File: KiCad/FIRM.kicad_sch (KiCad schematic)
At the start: 98 parts, among them J1 Conn_01x02_Pin, J2 DM3CS-SF, Q2 IRLML6402, SW1 PTS815, U1 STM32F405RGTx, U2 MIC5219-3.3YM5, U6 A-USBC-20F0-EA-GSR05, U7 W25Q128JVS, X2 32.768khz, Y1 12 MHz

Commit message: Finish part numbers
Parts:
- C1, C15, C19, C2, C20, C21, C25, C26, C27, C3, C4, C5, C8: LCSC PN  C1590 -> (none); MPN (none) -> C1590
- C10, C9: LCSC PN  C1607 -> (none); MPN (none) -> C1607
- C11, C12: LCSC PN  C37474 -> (none); MPN (none) -> C37474
- C13, C14: LCSC PN  C5360816 -> (none); MPN (none) -> C5360816
- C16, C18: LCSC PN  C1592 -> (none); MPN (none) -> C1592
- C17, C22, C24: LCSC PN  C1691 -> (none); MPN (none) -> C1691
- C23: LCSC PN  C1620 -> (none); MPN (none) -> C1620
- C6: LCSC PN  C1705 -> (none); MPN (none) -> C1705
- C7: LCSC PN  C1589 -> (none); MPN (none) -> C1589
- D1: LCSC PN  C82544 -> (none); MPN (none) -> C82544
- D2: LCSC PN  C2293 -> (none); MPN (none) -> C2293
- D3: LCSC PN  C2296 -> (none); MPN (none) -> C2296
- D4: LCSC PN  C84256 -> (none); MPN (none) -> C84256
- D5: LCSC PN  C2297 -> (none); MPN (none) -> C2297
- FB1: LCSC PN  C3716596 -> (none); MPN (none) -> C3716596
- J2: LCSC PN  C202111 -> (none); MPN (none) -> C202111
- Q2: LCSC PN  C22367042 -> (none); MPN (none) -> C22367042
- R1, R8: LCSC PN  C177329 -> (none); MPN (none) -> C177329
- R10: LCSC PN  C177341 -> (none); MPN (none) -> C177341
- R11, R15: LCSC PN  C22369820 -> (none); MPN (none) -> C22369820
- R12: LCSC PN  C22369819 -> (none); MPN (none) -> C22369819
- R13, R14, R21, R7: LCSC PN  C22356465 -> (none); MPN (none) -> C22356465
- R18, R19: LCSC PN  C22356633 -> (none); MPN (none) -> C22356633
- R2, R3, R4, R5, R6: LCSC PN  C177336 -> (none); MPN (none) -> C177336
- R20: LCSC PN  C177347 -> (none); MPN (none) -> C177347
- R22, R9: LCSC PN  C177348 -> (none); MPN (none) -> C177348
- SW1: LCSC PN  C411883 -> (none); MPN (none) -> C411883
- U1: LCSC PN  C15742 -> (none); MPN (none) -> C15742
- U2: LCSC PN  C5370977 -> (none); MPN (none) -> C5370977
- U3: LCSC PN  C22459454 -> (none); MPN (none) -> C22459454
- U4: LCSC PN  C404329 -> (none); MPN (none) -> C404329
- U5: LCSC PN  C5362283 -> (none); MPN (none) -> C5362283
- U6: LCSC PN  C22036153 -> (none); MPN (none) -> C22036153
- U7: LCSC PN  C97521 -> (none); MPN (none) -> C97521
- X2: LCSC PN  C2450425 -> (none); MPN (none) -> C2450425
- Y1: LCSC PN  C20625731 -> (none); MPN (none) -> C20625731
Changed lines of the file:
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@@
 			)
 		)
-		(property "LCSC PN " "C1590"
+		(property "MPN" "C1590"
 			(at 87.63 41.91 0)
 			(effects
@@
 			)
 		)
-		(property "LCSC PN " "C1590"
+		(property "MPN" "C1590"
 			(at 36.83 41.91 0)
 			(effects
@@
 			)
 		)
-		(property "LCSC PN " "C22356465"
+		(property "MPN" "C22356465"
 			(at 22.86 255.27 0)
 			(effects
@@
 			)
 		)
-		(property "LCSC PN " "C177329"
+		(property "MPN" "C177329"
 			(at 30.48 66.04 0)
 			(effects
@@
 			)
 		)
-		(property "LCSC PN " "C1691"
+		(property "MPN" "C1691"
 			(at 308.61 224.79 0)
 			(effects
@@
 			)
 		)
-		(property "LCSC PN " "C97521"
+		(property "MPN" "C97521"
 			(at 60.96 260.35 0)
 			(effects
@@
 			)
 		)
-		(property "LCSC PN " "C1590"
+		(property "MPN" "C1590"
 			(at 19.05 60.96 0)
 			(effects
@@
 			)
 		)
-		(property "LCSC PN " "C177336"
+		(property "MPN" "C177336"
 			(at 52.07 177.8 0)
 			(effects
@@
 			)
 		)
-		(property "LCSC PN " "C2296"
+		(property "MPN" "C2296"
 			(at 184.15 119.38 0)
 			(effects
@@
 			)
 		)
-		(property "LCSC PN " "C404329"
+		(property "MPN" "C404329"
 			(at 325.12 111.76 0)
 			(effects
@@
 			)
 		)
-		(property "LCSC PN " "C1590"
+		(property "MPN" "C1590"
 			(at 64.77 195.58 0)
 			(effects
@@
 			)
 		)
-		(property "LCSC PN " "C177336"
+		(property "MPN" "C177336"
 			(at 59.69 177.8 0)
 			(effects
@@
 			)
 		)
-		(property "LCSC PN " "C177336"
+		(property "MPN" "C177336"
 			(at 25.4 177.8 0)
 			(effects
@@
 			)
 		)
-		(property "LCSC PN " "C22356633"
+		(property "MPN" "C22356633"
 			(at 153.67 111.76 0)
 			(effects
@@
 			)
 		)
-		(property "LCSC PN " "C22356465"
+		(property "MPN" "C22356465"
 			(at 38.1 212.09 90)
 			(effects
@@
 			)
 		)
-		(property "LCSC PN " "C1590"
+		(property "MPN" "C1590"
 			(at 66.04 240.03 90)
 			(effects
@@
 			)
 		)
-		(property "LCSC PN " "C5360816"
+		(property "MPN" "C5360816"
 			(at 41.91 88.9 0)
 			(effects
@@
 			)
 		)
-		(property "LCSC PN " "C1590"
+		(property "MPN" "C1590"
 			(at 142.24 41.91 0)
 			(effects
@@
 			)
 		)
-		(property "LCSC PN " "C84256"
+		(property "MPN" "C84256"
 			(at 184.15 130.81 0)
 			(effects
@@
 			)
 		)
-		(property "LCSC PN " "C177341"
+		(property "MPN" "C177341"
 			(at 170.18 107.95 90)
 			(effects
@@
 			)
 		)
-		(property "LCSC PN " "C22356633"
+		(property "MPN" "C22356633"
 			(at 144.78 111.76 0)
 			(effects
@@
 			)
 		)
-		(property "LCSC PN " "C5360816"
+		(property "MPN" "C5360816"
 			(at 63.5 90.17 0)
 			(effects
@@
 			)
 		)
-		(property "LCSC PN " "C22369820"
+		(property "MPN" "C22369820"
 			(at 290.83 208.28 0)
 			(effects
@@
 			)
 		)
-		(property "LCSC PN " "C22369819"
+		(property "MPN" "C22369819"
 			(at 170.18 130.81 90)
 			(effects
@@
 			)
 		)
-		(property "LCSC PN " "C37474"
+		(property "MPN" "C37474"
 			(at 39.37 130.81 0)
 			(effects
@@
 			)
 		)
-		(property "LCSC PN " "C177336"
+		(property "MPN" "C177336"
 			(at 44.45 177.8 0)
 			(effects
@@
 			)
 		)
-		(property "LCSC PN " "C1691"
+		(property "MPN" "C1691"
 			(at 317.5 138.43 90)
 			(effects
@@
 			)
 		)
-		(property "LCSC PN " "C177347"
+		(property "MPN" "C177347"
 			(at 379.73 53.34 90)
 			(effects
@@
 			)
 		)
-		(property "LCSC PN " "C22356465"
+		(property "MPN" "C22356465"
 			(at 39.37 245.11 0)
 			(effects
@@
 			)
 		)
-		(property "LCSC PN " "C1607"
+		(property "MPN" "C1607"
 			(at 73.66 130.81 0)
 			(effects
@@
 			)
 		)
-		(property "LCSC PN " "C1592"
+		(property "MPN" "C1592"
 			(at 172.72 41.91 0)
 			(effects
@@
 			)
 		)
-		(property "LCSC PN " "C1590"
+		(property "MPN" "C1590"
 			(at 327.66 27.94 90)
 			(effects
@@
 			)
 		)
-		(property "LCSC PN " "C1589"
+		(property "MPN" "C1589"
 			(at 130.81 41.91 0)
 			(effects
@@
 			)
 		)
-		(property "LCSC PN " "C2450425"
+		(property "MPN" "C2450425"
 			(at 44.45 121.92 0)
 			(effects
@@
 			)
 		)
-		(property "LCSC PN " "C22036153"
+		(property "MPN" "C22036153"
 			(at 345.44 204.47 0)
 			(effects
@@
 			)
 		)
-		(property "LCSC PN " "C37474"
+		(property "MPN" "C37474"
 			(at 50.8 130.81 0)
 			(effects
@@
 			)
 		)
-		(property "LCSC PN " "C177329"
+		(property "MPN" "C177329"
 			(at 243.84 222.25 0)
 			(effects
@@
 			)
 		)
-		(property "LCSC PN " "C3716596"
+		(property "MPN" "C3716596"
 			(at 154.94 36.83 90)
 			(effects
@@
 			)
 		)
-		(property "LCSC PN " "C20625731"
+		(property "MPN" "C20625731"
 			(at 52.07 81.28 0)
 			(effects
@@
 			)
 		)
-		(property "LCSC PN " "C2297"
+		(property "MPN" "C2297"
 			(at 294.64 201.93 0)
 			(effects
@@
 			)
 		)
-		(property "LCSC PN " "C82544"
+		(property "MPN" "C82544"
 			(at 252.73 214.63 0)
 			(effects
@@
 			)
 		)
-		(property "LCSC PN " "C1590"
+		(property "MPN" "C1590"
 			(at 48.26 41.91 0)
 			(effects
@@
 			)
 		)
-		(property "LCSC PN " "C1691"
+		(property "MPN" "C1691"
 			(at 261.62 224.79 0)
 			(effects
@@
 			)
 		)
-		(property "LCSC PN " "C177336"
+		(property "MPN" "C177336"
 			(at 33.02 177.8 0)
 			(effects
@@
 			)
 		)
-		(property "LCSC PN " "C5362283"
+		(property "MPN" "C5362283"
 			(at 327.66 48.26 0)
 			(effects
@@
 			)
 		)
-		(property "LCSC PN " "C2293"
+		(property "MPN" "C2293"
 			(at 184.15 107.95 0)
 			(effects
@@
 			)
 		)
-		(property "LCSC PN " "C1590"
+		(property "MPN" "C1590"
 			(at 320.04 27.94 90)
 			(effects
@@
 			)
 		)
-		(property "LCSC PN " "C15742"
+		(property "MPN" "C15742"
 			(at 106.68 96.52 0)
 			(effects
@@
 			)
 		)
-		(property "LCSC PN " "C177348"
+		(property "MPN" "C177348"
 			(at 373.38 198.12 90)
 			(effects
@@
 			)
 		)
-		(property "LCSC PN " "C5370977"
+		(property "MPN" "C5370977"
 			(at 280.67 217.17 0)
 			(effects
@@
 			)
 		)
-		(property "LCSC PN " "C177348"
+		(property "MPN" "C177348"
 			(at 367.03 195.58 90)
 			(effects
@@
 			)
 		)
-		(property "LCSC PN " "C1592"
+		(property "MPN" "C1592"
 			(at 314.96 148.59 0)
 			(effects
@@
 			)
 		)
-		(property "LCSC PN " "C1590"
+		(property "MPN" "C1590"
 			(at 73.66 41.91 0)
 			(effects
@@
 			)
 		)
-		(property "LCSC PN " "C1705"
+		(property "MPN" "C1705"
 			(at 22.86 41.91 0)
 			(effects
@@
 			)
 		)
-		(property "LCSC PN " "C22369820"
+		(property "MPN" "C22369820"
 			(at 170.18 119.38 90)
 			(effects
@@
 			)
 		)
-		(property "LCSC PN " "C22459454"
+		(property "MPN" "C22459454"
 			(at 251.46 55.88 0)
 			(effects
@@
 			)
 		)
-		(property "LCSC PN " "C22367042"
+		(property "MPN" "C22367042"
 			(at 259.08 201.93 0)
 			(effects
@@
 			)
 		)
-		(property "LCSC PN " "C1590"
+		(property "MPN" "C1590"
 			(at 254 76.2 0)
 			(effects
@@
 			)
 		)
-		(property "LCSC PN " "C1607"
+		(property "MPN" "C1607"
 			(at 62.23 130.81 0)
 			(effects
@@
 			)
 		)
-		(property "LCSC PN " "C202111"
+		(property "MPN" "C202111"
 			(at 96.52 196.85 0)
 			(effects
@@
 			)
 		)
-		(property "LCSC PN " "C1590"
+		(property "MPN" "C1590"
 			(at 60.96 41.91 0)
 			(effects
@@
 			)
 		)
-		(property "LCSC PN " "C22356465"
+		(property "MPN" "C22356465"
 			(at 33.02 255.27 0)
 			(effects
@@
 			)
 		)
-		(property "LCSC PN " "C411883"
+		(property "MPN" "C411883"
 			(at 382.27 31.75 0)
 			(effects
@@
 			)
 		)
-		(property "LCSC PN " "C1620"
+		(property "MPN" "C1620"
 			(at 290.83 222.25 0)
 			(effects
@@
 			)
 		)
-		(property "LCSC PN " "C1590"
+		(property "MPN" "C1590"
 			(at 264.16 76.2 0)
 			(effects

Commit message: bom digikey
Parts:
- C1, C15, C19, C2, C20, C21, C25, C26, C27, C3, C4, C5, C8: Digikey PN (none) -> 399-C0603C104K5RACTUCT-ND
- C10, C9: Digikey PN (none) -> 490-4520-1-ND
- C11, C12: Digikey PN (none) -> 1276-2134-1-ND
- C13, C14: Digikey PN (none) -> 311-1767-1-ND
- C16, C18: Digikey PN (none) -> 1276-1184-1-ND
- C17, C22, C24: Digikey PN (none) -> 490-18214-1-ND
- C23: Digikey PN (none) -> 1276-1168-1-ND
- C6: Digikey PN (none) -> 1276-1044-1-ND
- C7: Digikey PN (none) -> 399-C0603C103K5RACTUCT-ND
- D1: Digikey PN (none) -> 1N5819HW-FDICT-ND
- D2: Digikey PN (none) -> 160-1645-1-ND
- D3: Digikey PN (none) -> 160-1428-1-ND
- D4: Digikey PN (none) -> 160-1422-1-ND
- D5: Digikey PN (none) -> 160-1423-1-ND
- FB1: Digikey PN (none) -> 1934-1472-1-ND
- J2: Digikey PN (none) -> HR1972CT-ND
- Q2: Digikey PN (none) -> IRLML6402PBFCT-ND
- R1, R8: Digikey PN (none) -> 311-100KHRCT-ND
- R10: Digikey PN (none) -> 311-330HRCT-ND
- R11, R15: Digikey PN (none) -> P1.2KDBCT-ND
- R12: Digikey PN (none) -> 311-1.50KHRCT-ND
- R13, R14, R21, R7: Digikey PN (none) -> 311-10.0KHRCT-ND
- R18, R19: Digikey PN (none) -> 311-2.20KHRCT-ND
- R2, R3, R4, R5, R6: Digikey PN (none) -> 311-47.0KHRCT-ND
- R20: Digikey PN (none) -> 541-100HCT-ND
- R22, R9: Digikey PN (none) -> 311-5.10KHRCT-ND
- SW1: Digikey PN (none) -> CKN12215-1-ND
- U1: Digikey PN (none) -> 497-11767-ND
- U2: Digikey PN (none) -> 576-1281-1-ND
- U3: Digikey PN (none) -> 1428-ICM-45686CT-ND
- U4: Digikey PN (none) -> 1267-MMC5983MACT-ND
- U5: Digikey PN (none) -> 828-BMP581CT-ND
- U6: Digikey PN (none) -> 123-A-USBC-20F0-EA-GSR05CT-ND
- U7: Digikey PN (none) -> 256-W25Q128JVSIQTRCT-ND
- X2: Digikey PN (none) -> 50-ECS-.327-6-34R-TRCT-ND
- Y1: Digikey PN (none) -> 535-ABM8-272-T3CT-ND

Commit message: update bom
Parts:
- C16, C18: Digikey PN 1276-1184-1-ND -> 1276-1029-1-ND
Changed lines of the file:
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@@
 			)
 		)
-		(property "Digikey PN" "1276-1184-1-ND"
+		(property "Digikey PN" "1276-1029-1-ND"
 			(at 172.72 41.91 0)
 			(effects
@@
 			)
 		)
-		(property "Digikey PN" "1276-1184-1-ND"
+		(property "Digikey PN" "1276-1029-1-ND"
 			(at 314.96 148.59 0)
 			(effects

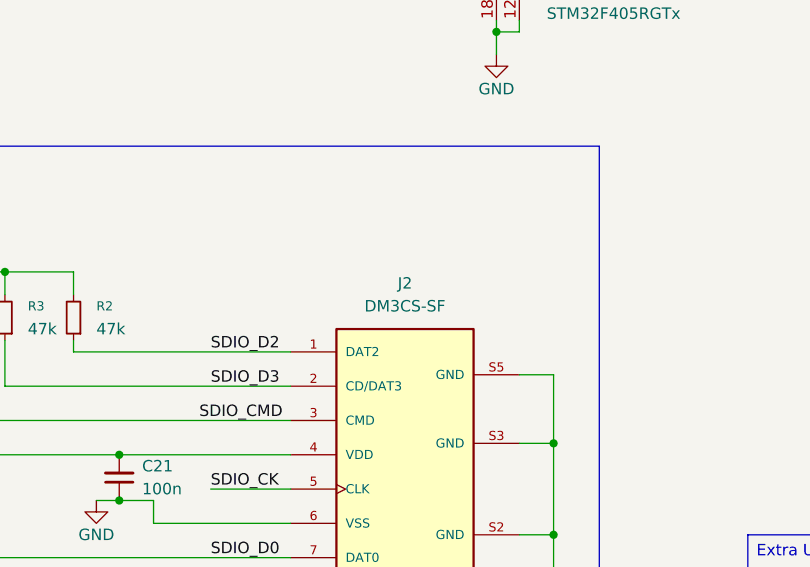
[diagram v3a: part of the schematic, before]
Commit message: fix fb and cap
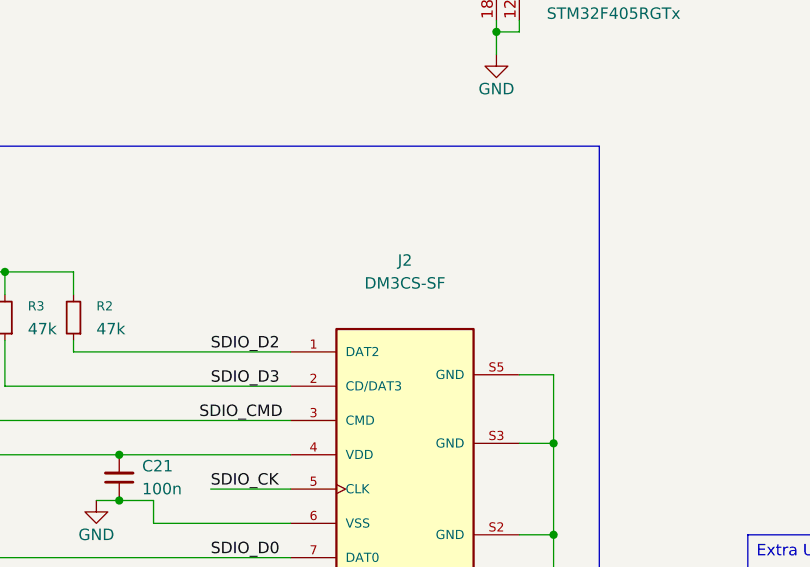
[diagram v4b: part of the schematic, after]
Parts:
- C16, C18: Digikey PN 1276-1029-1-ND -> 587-1241-1-ND
- FB1: footprint Inductor_SMD:L_1206_3216Metric -> Inductor_SMD:L_0805_2012Metric
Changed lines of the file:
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@@
 			)
 		)
-		(property "Digikey PN" "1276-1029-1-ND"
+		(property "Digikey PN" "587-1241-1-ND"
 			(at 172.72 41.91 0)
 			(effects
@@
 			)
 		)
-		(property "Footprint" "Inductor_SMD:L_1206_3216Metric"
+		(property "Footprint" "Inductor_SMD:L_0805_2012Metric"
 			(at 154.94 38.608 90)
 			(effects
@@
 			)
 		)
-		(property "Digikey PN" "1276-1029-1-ND"
+		(property "Digikey PN" "587-1241-1-ND"
 			(at 314.96 148.59 0)
 			(effects
@@
 		(fields_autoplaced yes)
 		(property "Reference" "J2"
-			(at 96.52 173.99 0)
+			(at 96.52 171.45 0)
 			(effects
 				(font
@@
 		)
 		(property "Value" "DM3CS-SF"
-			(at 96.52 176.53 0)
+			(at 96.52 173.99 0)
 			(effects
 				(font
@@
 		)
 		(property "Footprint" "DM3CS-SF:HRS_DM3CS-SF"
-			(at 96.52 196.85 0)
+			(at 96.52 176.53 0)
 			(effects
 				(font
 					(size 1.27 1.27)
 				)
-				(justify bottom)
 				(hide yes)
 			)

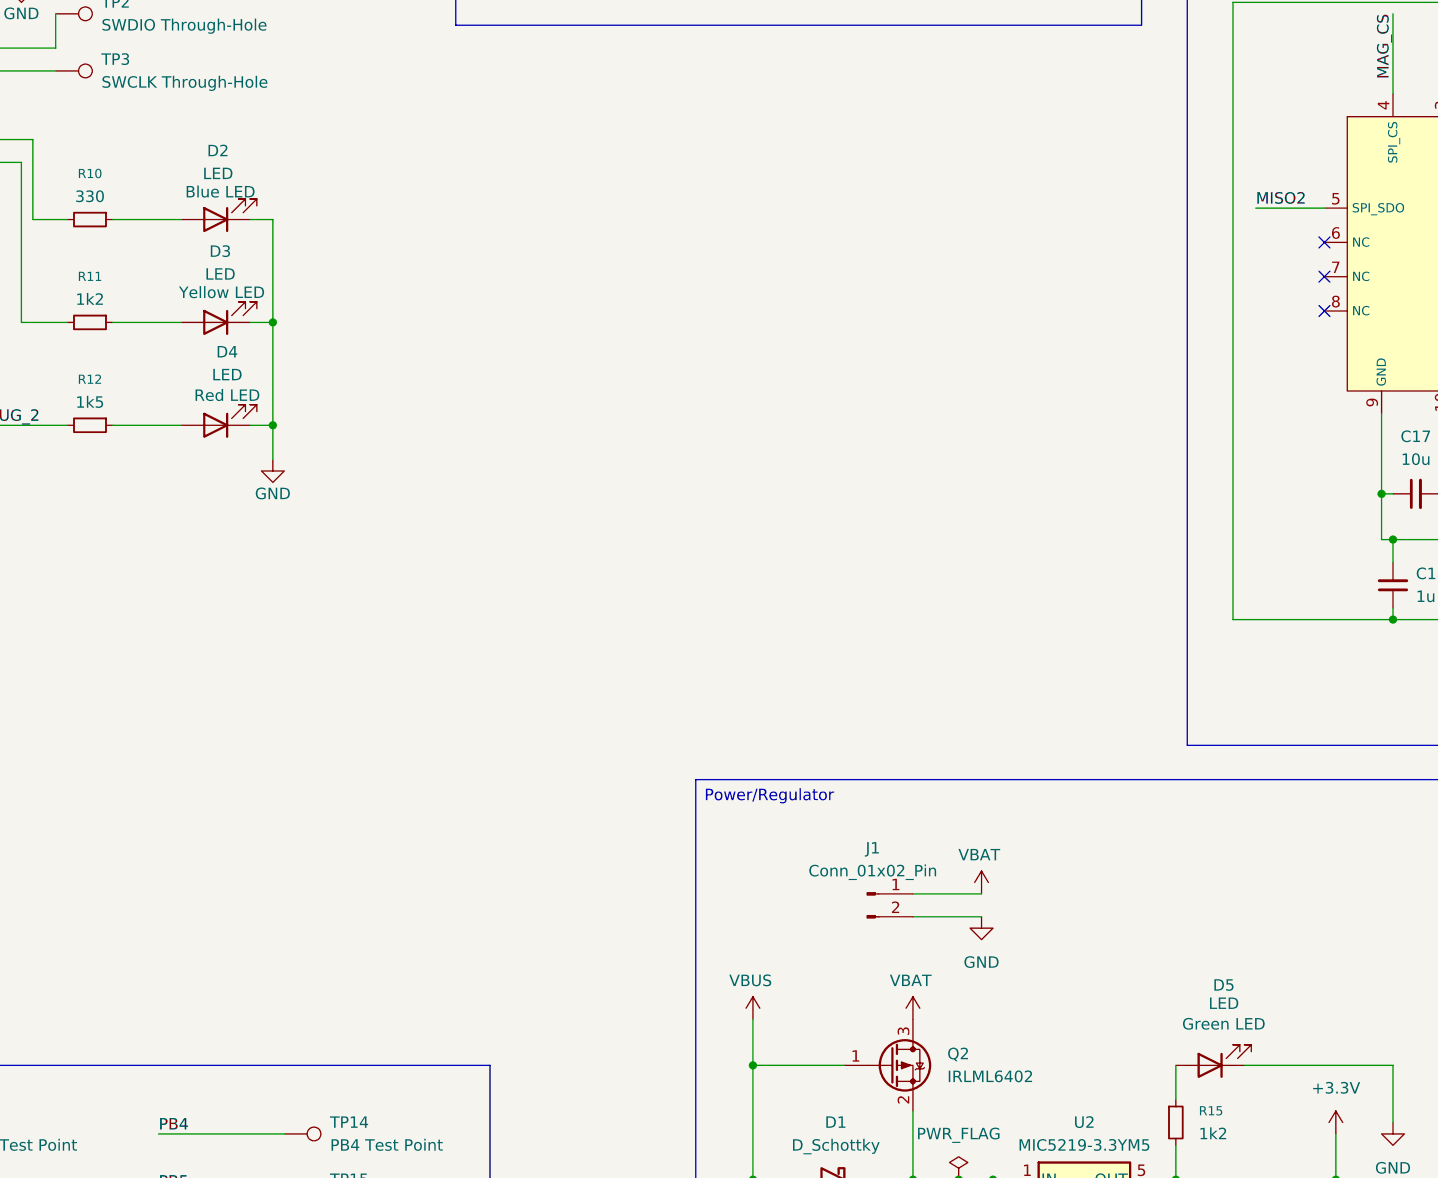
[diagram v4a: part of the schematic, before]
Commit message: Pick and place fixes
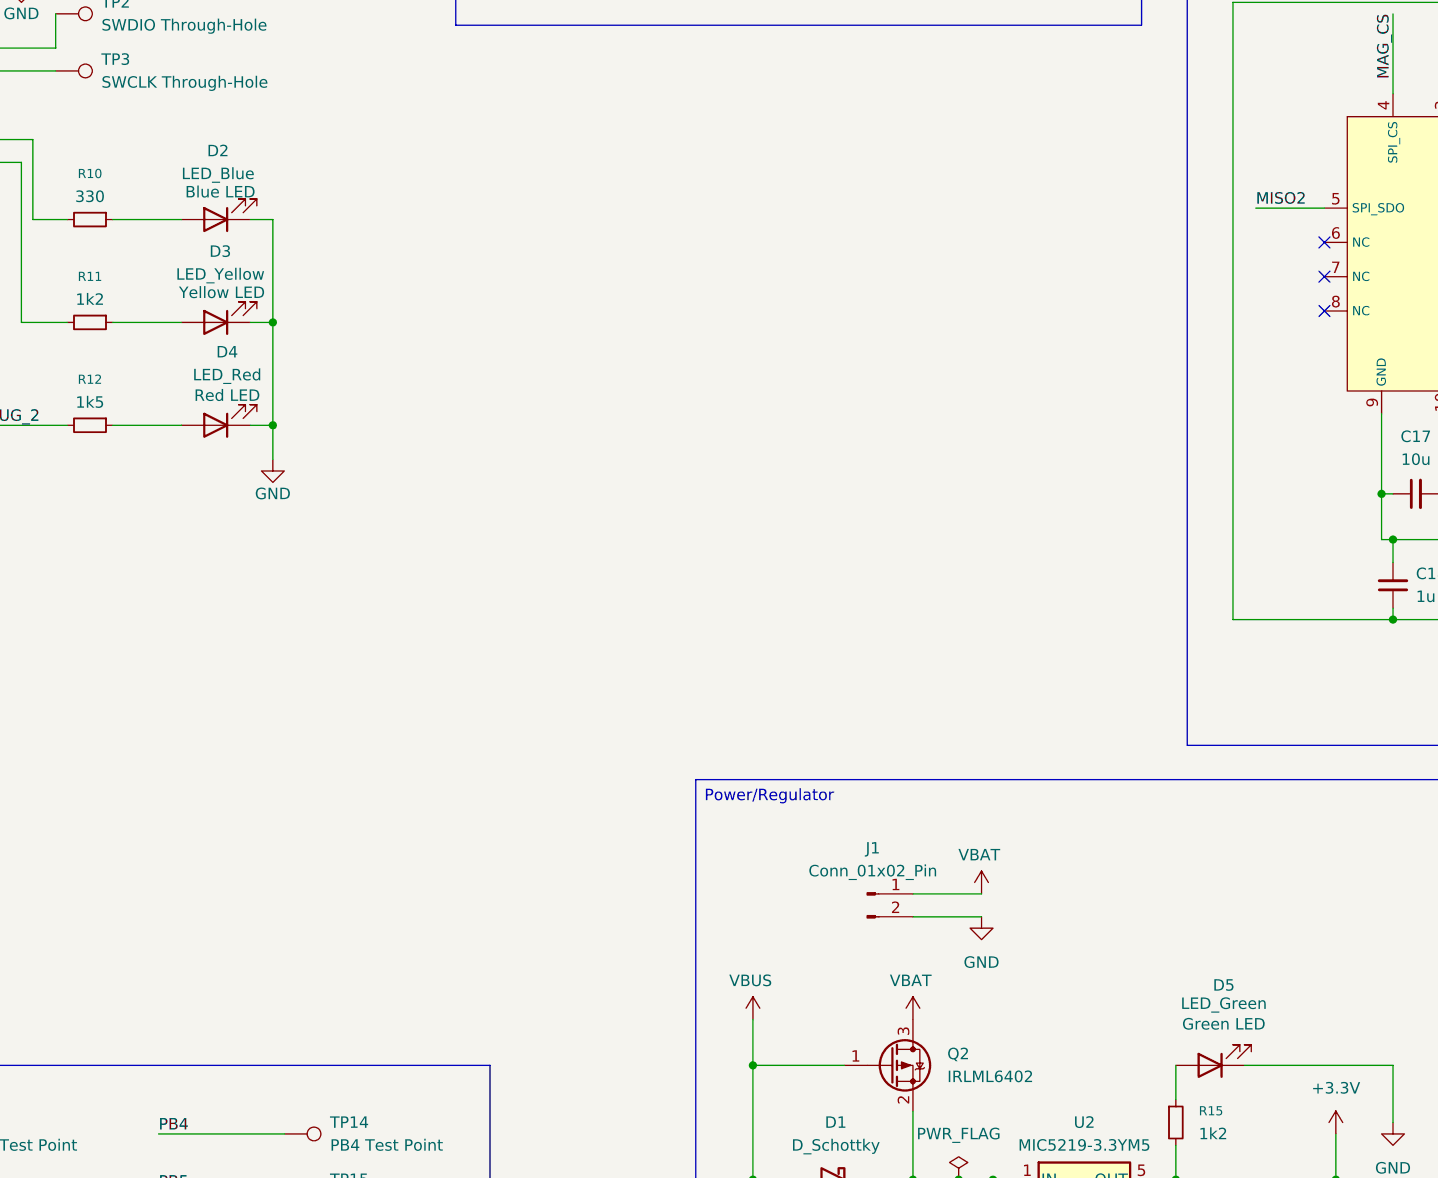
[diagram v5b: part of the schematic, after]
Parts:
- D2: value LED -> LED_Blue
- D3: value LED -> LED_Yellow
- D4: value LED -> LED_Red
- D5: value LED -> LED_Green
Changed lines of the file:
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@@
 			)
 		)
-		(property "Value" "LED"
+		(property "Value" "LED_Yellow"
 			(at 184.658 114.046 0)
 			(effects
@@
 			)
 		)
-		(property "Value" "LED"
+		(property "Value" "LED_Red"
 			(at 185.42 125.222 0)
 			(effects
@@
 			)
 		)
-		(property "Value" "LED"
+		(property "Value" "LED_Green"
 			(at 296.164 195.072 0)
 			(effects
@@
 			)
 		)
-		(property "Value" "LED"
+		(property "Value" "LED_Blue"
 			(at 184.404 102.87 0)
 			(effects
